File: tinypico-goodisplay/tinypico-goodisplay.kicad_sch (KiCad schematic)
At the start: 23 parts, among them Q1 Si1308, U1 TinypicoESP32_Symbol, U2 FPCConn

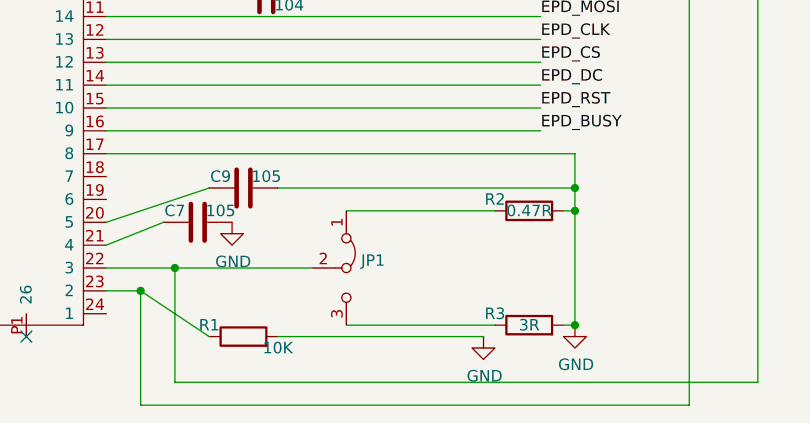
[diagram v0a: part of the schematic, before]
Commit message: Do not exclude C8 from POS files
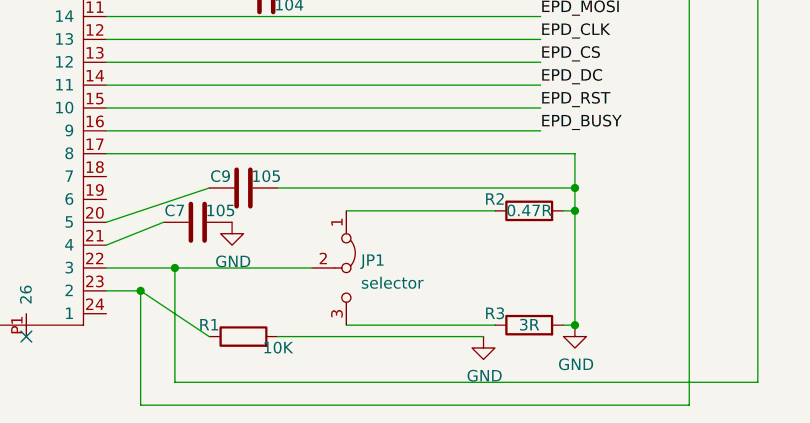
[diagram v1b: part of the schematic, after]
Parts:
- JP1: value (none) -> selector; footprint (none) -> footprint:switch-MK-12C02-G020
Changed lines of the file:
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@@
       (effects (font (size 1.27 1.27)) (justify left))
     )
-    (property "Value" "" (id 1) (at 86.7162 154.1022 90)
+    (property "Value" "selector" (id 1) (at 86.7162 154.1022 90)
       (effects (font (size 1.27 1.27)) (justify left))
     )
-    (property "Footprint" "" (id 2) (at 85.09 152.4 0)
+    (property "Footprint" "footprint:switch-MK-12C02-G020" (id 2) (at 85.09 152.4 0)
       (effects (font (size 1.27 1.27)) hide)
     )

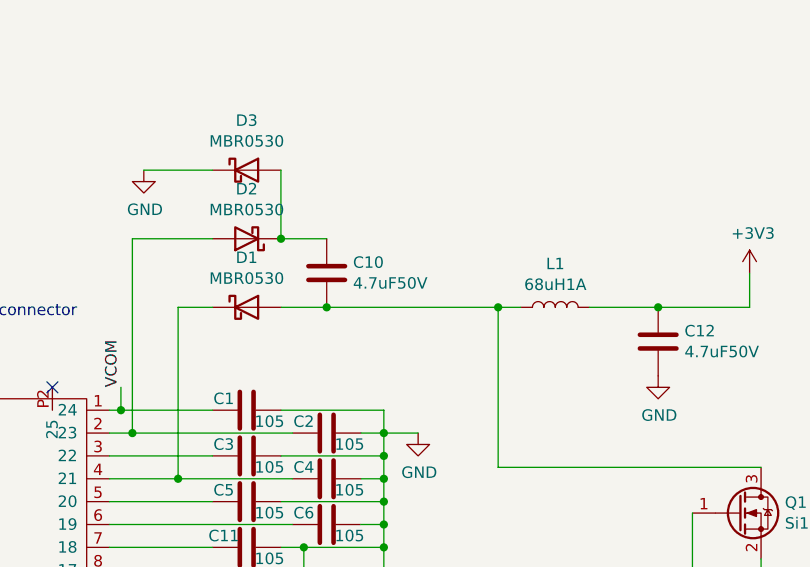
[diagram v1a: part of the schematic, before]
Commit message: Capacitor btw. diodes is 4.7uF not 470nF
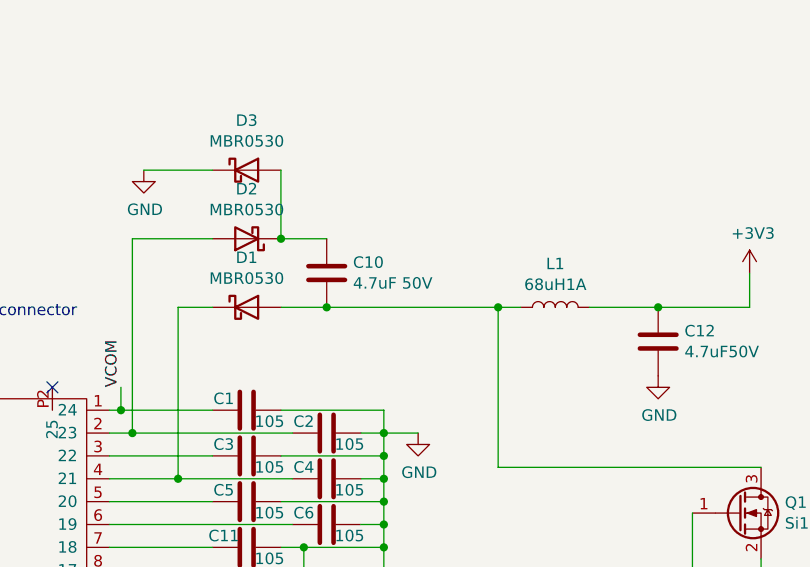
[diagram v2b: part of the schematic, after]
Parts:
- C10: value 4.7uF50V -> 4.7uF 50V; LCSC C13967 -> C1779
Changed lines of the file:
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@@
       (effects (font (size 1.27 1.27)) (justify right))
     )
-    (property "Value" "4.7uF50V" (id 1) (at 85.471 84.963 0)
+    (property "Value" "4.7uF 50V" (id 1) (at 85.471 84.963 0)
       (effects (font (size 1.27 1.27)) (justify right))
     )
@@
       (effects (font (size 1.27 1.27)) hide)
     )
-    (property "LCSC" "C13967" (id 4) (at 82.55 83.82 0)
+    (property "LCSC" "C1779" (id 4) (at 82.55 83.82 0)
       (effects (font (size 1.27 1.27)) hide)
     )
@@
     )
     (path "/00000000-0000-0000-0000-0000606b8743"
-      (reference "C10") (unit 1) (value "4.7uF50V") (footprint "Capacitor_SMD:C_0805_2012Metric_Pad1.18x1.45mm_HandSolder")
+      (reference "C10") (unit 1) (value "4.7uF 50V") (footprint "Capacitor_SMD:C_0805_2012Metric_Pad1.18x1.45mm_HandSolder")
     )
     (path "/00000000-0000-0000-0000-0000606b4d66"

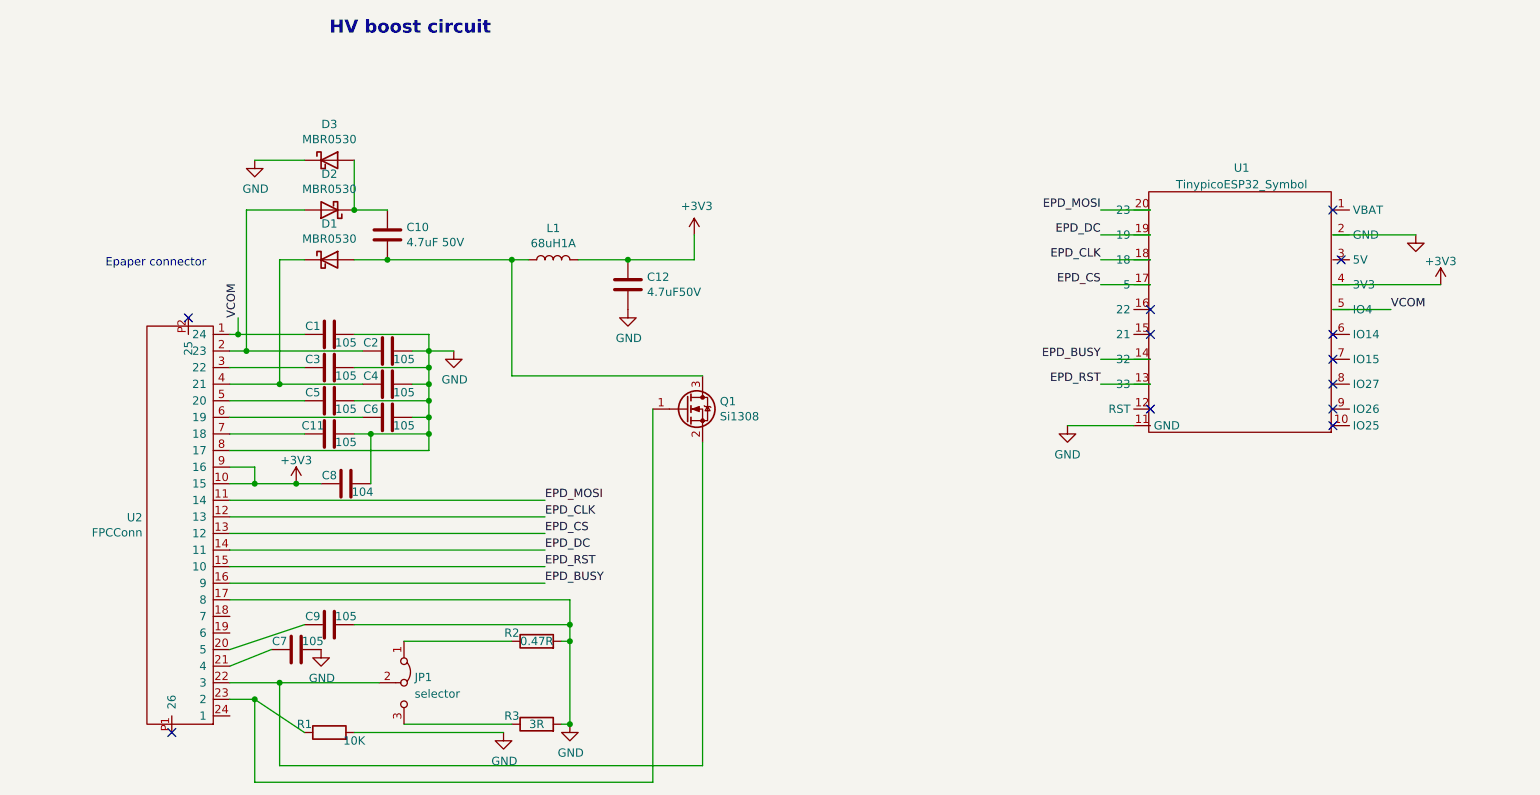
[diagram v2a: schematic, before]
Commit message: Update tinypico adapter
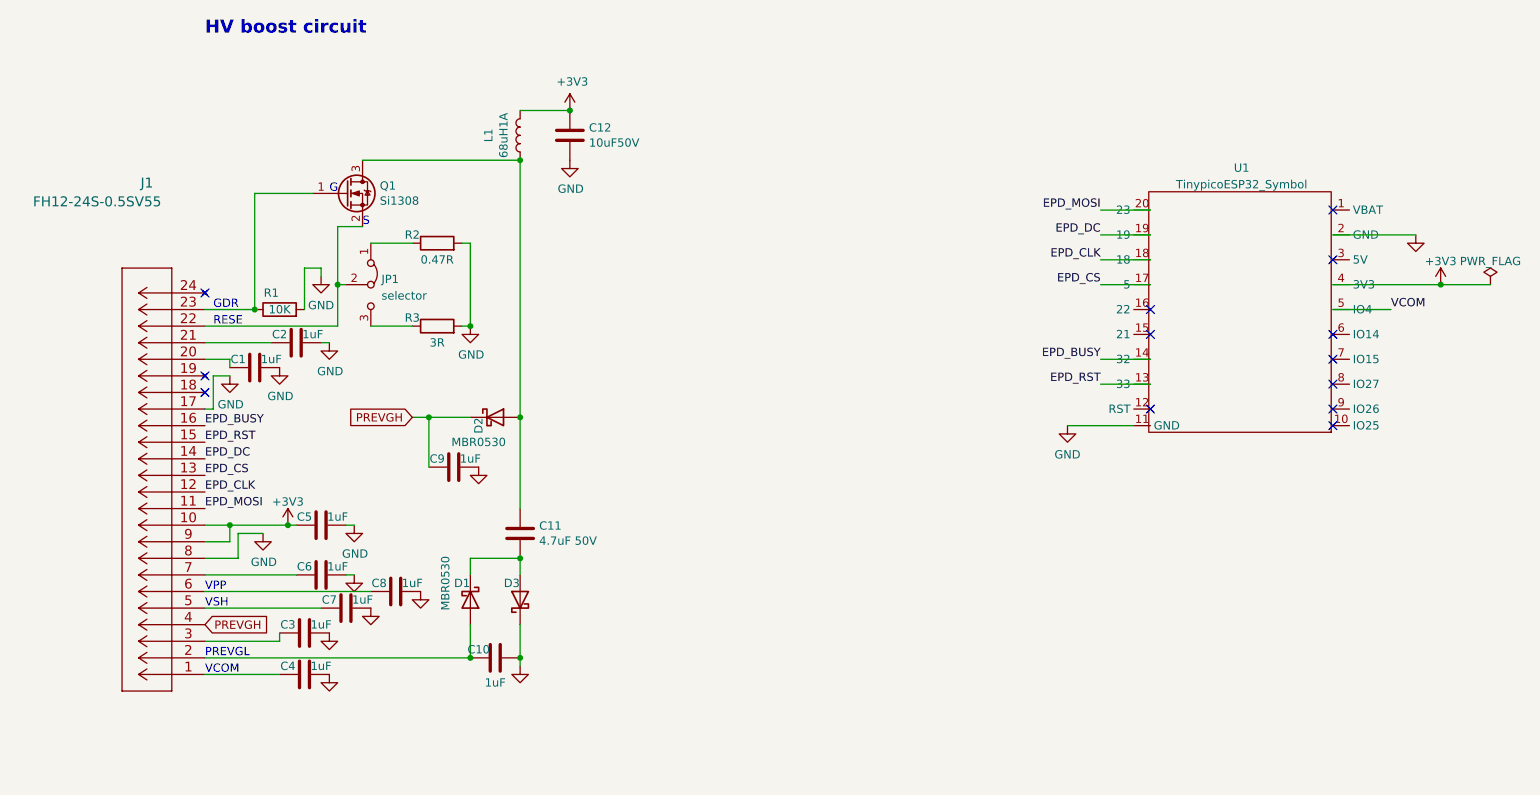
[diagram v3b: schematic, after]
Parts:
- removed U2: FPCConn, footprint:Hirose_FH12-24S-0.5SH_1x24-1MP_P0.50mm_Horizontal, symbol M5StampC3-rescue:FPCConn-Connector2
- added J1: FH12-24S-0.5SV55, footprint:Hirose_FH12-24S-0.5SH_1x24-1MP_P0.50mm_Horizontal, symbol footprint:FH12-24S-0.5SV55
- C1, C2, C3, C4, C5, C6, C7, C9: value 105 -> 1uF
- C10: value 4.7uF 50V -> 1uF; LCSC C1779 -> C28323
- C11: value 105 -> 4.7uF 50V; LCSC C28323 -> C1779
- C12: value 4.7uF50V -> 10uF50V; footprint Capacitor_SMD:C_0805_2012Metric_Pad1.18x1.45mm_HandSolder -> Capacitor_SMD:C_0603_1608Metric; LCSC C13967 -> C96446
- C8: value 104 -> 1uF; LCSC C49678 -> C28323
- R2: footprint Resistor_SMD:R_0805_2012Metric_Pad1.20x1.40mm_HandSolder -> Resistor_SMD:R_0603_1608Metric; LCSC C25040 -> C103895
- R3: footprint (none) -> Resistor_SMD:R_0603_1608Metric; LCSC C247097 -> C25237
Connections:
- net +3V3: now also C5.2, J1.10, J1.9; no longer C8.2
- net EPD_BUSY: now also J1.16
- net EPD_CLK: now also J1.12
- net EPD_CS: now also J1.13
- net EPD_DC: now also J1.14
- net EPD_MOSI: now also J1.11
- net EPD_RST: now also J1.15
- net GND: now also C10.1, J1.17, J1.8; no longer C11.1
- net VCOM: no longer C1.2
- net at D2.2 (A): now also C11.2, L1.1, Q1.3 (D); no longer C2.2
- net at C4.2: now also J1.1; no longer D1.1 (K)
- net at Q1.1 (G), R1.1: now also J1.23
- net at JP1.2 (C), Q1.2 (S): now also J1.22
- net at C3.2: now also J1.3
- net at C6.2: now also J1.7
- net PREVGH: now reaches C9.2
- net PREVGH: now also D2.1 (K), J1.4
- net at C7.2: now also J1.5
- new net: C10.2, D1.2 (A), J1.2
- new net: C1.2, J1.20
- new net: C2.2, J1.21
- new net: C8.2, J1.6
- new net: C11.1, D1.1 (K), D3.2 (A)
- no-connect marks 12 -> 13
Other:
- note added: "G"
- note added: "GDR"
- note added: "PREVGL"
- note added: "RESE"
- note added: "S"
- note added: "VCOM"
- note added: "VPP"
- note added: "VSH"
- note removed: "Epaper connector"
- moved on the sheet: C12, L1
